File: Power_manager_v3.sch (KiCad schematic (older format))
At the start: 100 parts, among them J1 L_input, J2 Pow_mng_pow, J3 Load1, J4 Load2, J5 SWD (PLS5), J6 Dig_mod_iface, Q1 2N5551S, Q2 2N5551S, Q3 BSS138, U1 DC12003, U2 G3MB-202PL, U3 G3MB-202PL, U4 STM32F030F4Px, U5 HLW8112, U6 ADuM1251ARZ, U7 ADuM1201AR, U8 LM1117-3.3, Y1 CSTCE8M, Y2 ABLS-3.579545MHZ-D-3-Y-T

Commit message: Окончена трассировка печатной платы
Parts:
- removed C14, C16: 470uF, Capacitor_Tantalum_SMD:CP_EIA-7343-31_Kemet-D, symbol Device:CP_Small
- removed C19, C25, C27, C32: 10uF, Capacitor_SMD:C_0603_1608Metric, symbol Device:C_Small
- removed C20, C24, C26, C28, C29, C30, C31: 100nF, Capacitor_SMD:C_0603_1608Metric, symbol Device:C_Small
- removed D6: LM66100DCKR, SOP65P210X110-6N, symbol Modules:LM66100DCKR
- removed D7: +3.3V, LED_SMD:LED_0603_1608Metric, symbol Device:LED
- removed GNDPWR1: GND, TestPoint:TestPoint_THTPad_D2.0mm_Drill1.0mm, symbol Connector:TestPoint_Small
- removed J6: Dig_mod_iface, Connector_PinSocket_1.27mm:PinSocket_2x05_P1.27mm_Horizontal, symbol Connector_Generic:Conn_02x05_Odd_Even
- removed JP3: BOOT0, Jumper:SolderJumper-2_P1.3mm_Open_RoundedPad1.0x1.5mm, symbol Jumper:Jumper_2_Open
- removed JP5: N_en, Jumper:SolderJumper-2_P1.3mm_Open_TrianglePad1.0x1.5mm, symbol Jumper:SolderJumper_2_Open
- removed PS1: B0505S, Modules:B0505S, symbol Modules:B0505S
- removed Q3: BSS138, Package_TO_SOT_SMD:SOT-23, symbol Transistor_FET:BSS138
- removed R25, R37: 10k, Resistor_SMD:R_0603_1608Metric, symbol Device:R_Small
- removed R26: 2.2M, Resistor_SMD:R_0603_1608Metric, symbol Device:R_Small
- removed U6: ADuM1251ARZ, Package_SO:SOIC-8_3.9x4.9mm_P1.27mm, symbol Modules:ADuM1251ARZ
- removed U7: ADuM1201AR, Package_SO:SOIC-8_3.9x4.9mm_P1.27mm, symbol Isolator:ADuM1201AR
- removed U8: LM1117-3.3, Package_TO_SOT_SMD:SOT-223-3_TabPin2, symbol Regulator_Linear:LM1117-3.3
- added D6: +3.3VP, LED_SMD:LED_0603_1608Metric, symbol Device:LED
- added J6: Dig_mod_iface, Connector_PinSocket_1.27mm:PinSocket_2x03_P1.27mm_Horizontal, symbol Connector_Generic:Conn_02x03_Odd_Even
- added JP2: N_en, Jumper:SolderJumper-2_P1.3mm_Open_TrianglePad1.0x1.5mm, symbol Jumper:SolderJumper_2_Open
- added JP4: Jumper_2x2_Open, Modules:PinHeader_2x02_P1.27mm_Vertical, symbol Modules:Jumper_2x2_Open
- added R14: 10k, Resistor_SMD:R_0603_1608Metric, symbol Device:R_Small
- added U4: DC5V_DC5V3V3_v3, Modules:DC5V_DC5V3V3_v3, symbol Modules:DC5V_DC5V3V3_v3
- added U7: ADuM_I2C_v3, Modules:ADuM_I2C_Horizontal, symbol Modules:ADuM_I2C_v3
- D5: value +5P -> +5V
- JP5: renamed from JP4; value 5VL_en -> 5VP_en
- JP6: value 3V3_en -> 3.3VP_en
- KP1: footprint TestPoint:TestPoint_Pad_1.0x1.0mm -> TestPoint:TestPoint_THTPad_D1.5mm_Drill0.7mm
- renumbered C15 to C14, C17 to C15, C18 to C16, C21 to C17, C22 to C18, C5 to C4, C6 to C5, C7 to C6, C8 to C7, C4 to C8, JP2 to JP3, R12 to R11, R13 to R12, R11 to R13, R14 to R15, R15 to R16, R16 to R17, R17 to R18, R18 to R19, R19 to R20, R20 to R21, R21 to R22, R22 to R23, R23 to R24, R24 to R25, R27 to R26, R28 to R27, U4 to U5, U5 to U6
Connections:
- net +5VL is gone; now on net +5VP: D1.2 (A), D2.2 (A), D3.1 (K), D4.1 (K), JP5.2 (B), U2.3 (+), U3.3 (+)
- net +3.3VP: now also C23.1, R14.2, U7.B1 (Vcc2)
- net +5P: now also U4.3 (+5Vout), U7.A5 (Vcc1); no longer C3.2, R13.2, U1.3 (Vcc)
- net +5VP: no longer J2.1 (Pin_1), J2.2 (Pin_2), JP3.2 (B)
- net +5V_state: now also J6.3 (Pin_3), U4.4 (+5Vstate), U7.A1 (ina1)
- net +5V_valid: now also U5.14 (PB1), U7.B5 (outa2); no longer U5.7 (PA1)
- net GND1: now also J6.1 (Pin_1), J6.2 (Pin_2), U4.2 (GND1), U7.A6 (GND1)
- net GNDPWR: now also C23.2, D6.1 (K), JP2.2 (B), JP4.1 (A), JP4.3 (A), U4.6 (GND2), U7.B2 (GND2); no longer J1.3 (Pin_3), U1.2 (N)
- net I2C_Int: now also J6.4 (Pin_4), U7.A2 (outb1)
- net I2C_SCL: now also U7.B4 (SCL2)
- net I2C_SDA: now also U7.B3 (SDA2)
- net Int: now also U7.B6 (inb2)
- net L1_o1_nEn: now also U5.7 (PA1); no longer U5.8 (PA2)
- net L1_o2_nEn: now also U5.8 (PA2); no longer U5.9 (PA3)
- net nRst: now also JP4.4 (B)
- net scl0: now also J6.5 (Pin_5), U7.A4 (SCL1)
- net sda0: now also J6.6 (Pin_6), U7.A3 (SDA1)
- net at JP6.1 (A): now also U4.7 (+3.3V2)
- net at R23.1, U5.1 (BOOT0): now also JP4.2 (B)
- net at KP1.1: now also U5.9 (PA3); no longer U5.14 (PB1)
- net at JP5.1 (A): now also U4.5 (+5V2); no longer C23.2
- net +5P0: no longer names the net of C6.2, C8.2
- net +5P0: now also JP3.2 (B), U4.1 (+5Vin); no longer JP3.1 (A)
- new net: J1.3 (Pin_3), JP2.1 (A), U1.2 (N)
- new net: D6.2 (A), R14.1
- new net +5V: C3.2, J2.1 (Pin_1), J2.2 (Pin_2), JP3.1 (A), R13.2, U1.3 (Vcc)
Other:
- moved on the sheet: C1, C10, C11, C12, C13, C14, C15, C16, C17, C18, C2, C3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

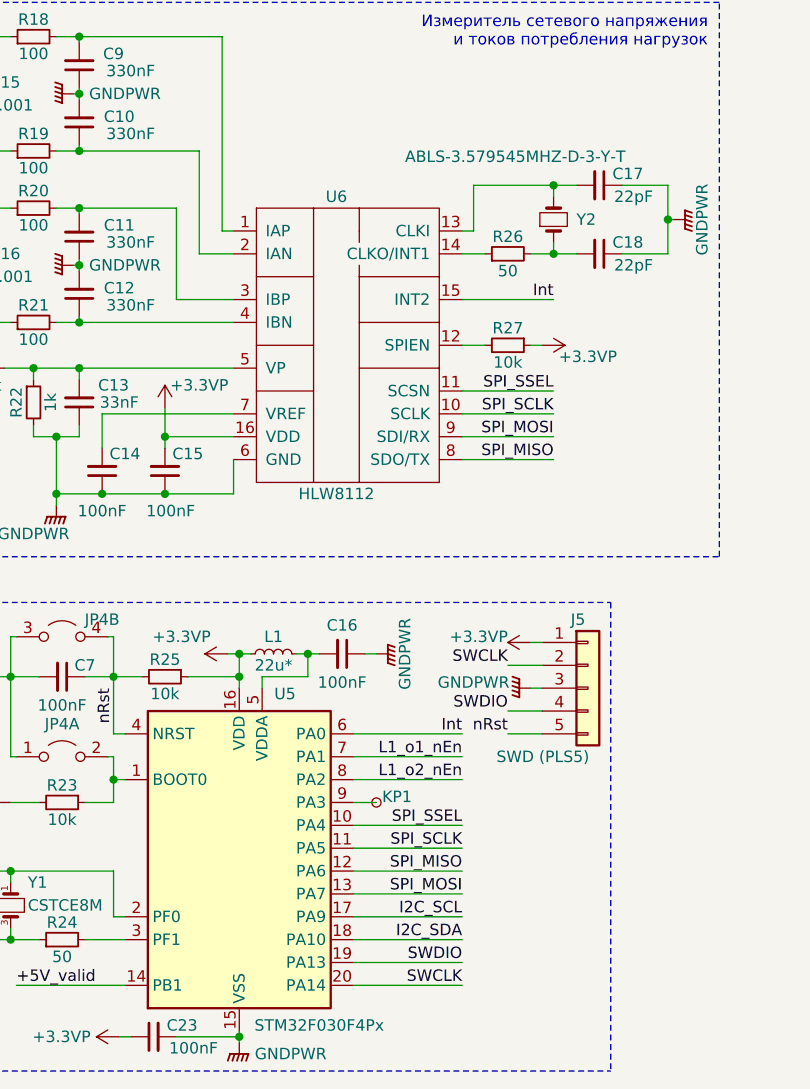
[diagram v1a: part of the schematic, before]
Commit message: Исправления в схеме и в печатной плате.
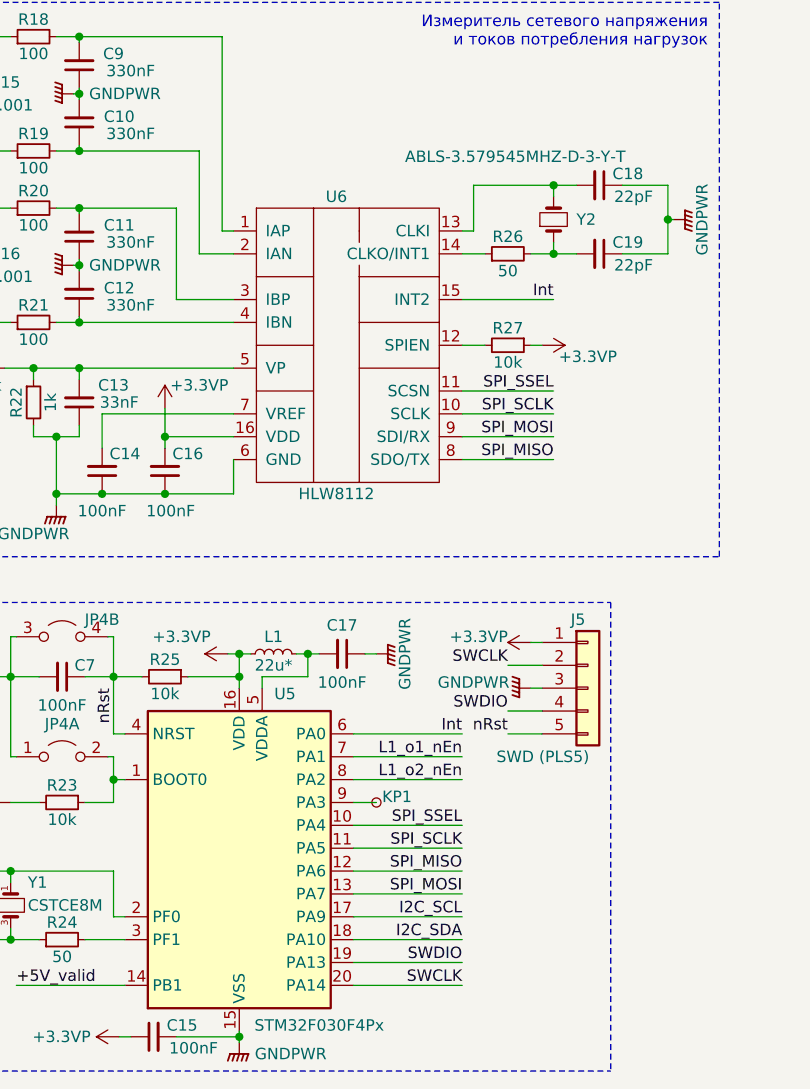
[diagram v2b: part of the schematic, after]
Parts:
- renumbered C23 to C15, C15 to C16, C16 to C17, C17 to C18, C18 to C19

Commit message: Мелкие исправления в схеме и плате
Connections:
- net +5P: now also J2.1 (Pin_1), J2.2 (Pin_2); no longer J2.5 (Pin_5), J2.6 (Pin_6)
- net +5V: now also J2.5 (Pin_5), J2.6 (Pin_6); no longer J2.1 (Pin_1), J2.2 (Pin_2)
- net +5V_state: now also J6.1 (Pin_1); no longer J6.3 (Pin_3)
- net GND1: now also J6.3 (Pin_3), J6.4 (Pin_4); no longer J6.1 (Pin_1), J6.2 (Pin_2)
- net I2C_Int: now also J6.2 (Pin_2); no longer J6.4 (Pin_4)
